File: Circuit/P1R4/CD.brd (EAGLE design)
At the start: 59.7 x 59.7 mm, 126 parts, among them U1 MK20DX256VLH7, U2 TPS61200, U3 MPU-9250, Y1 32.768KHz, Y2 16Mhz/8pF, Y3 26 Mhz, Y4 16 Mhz

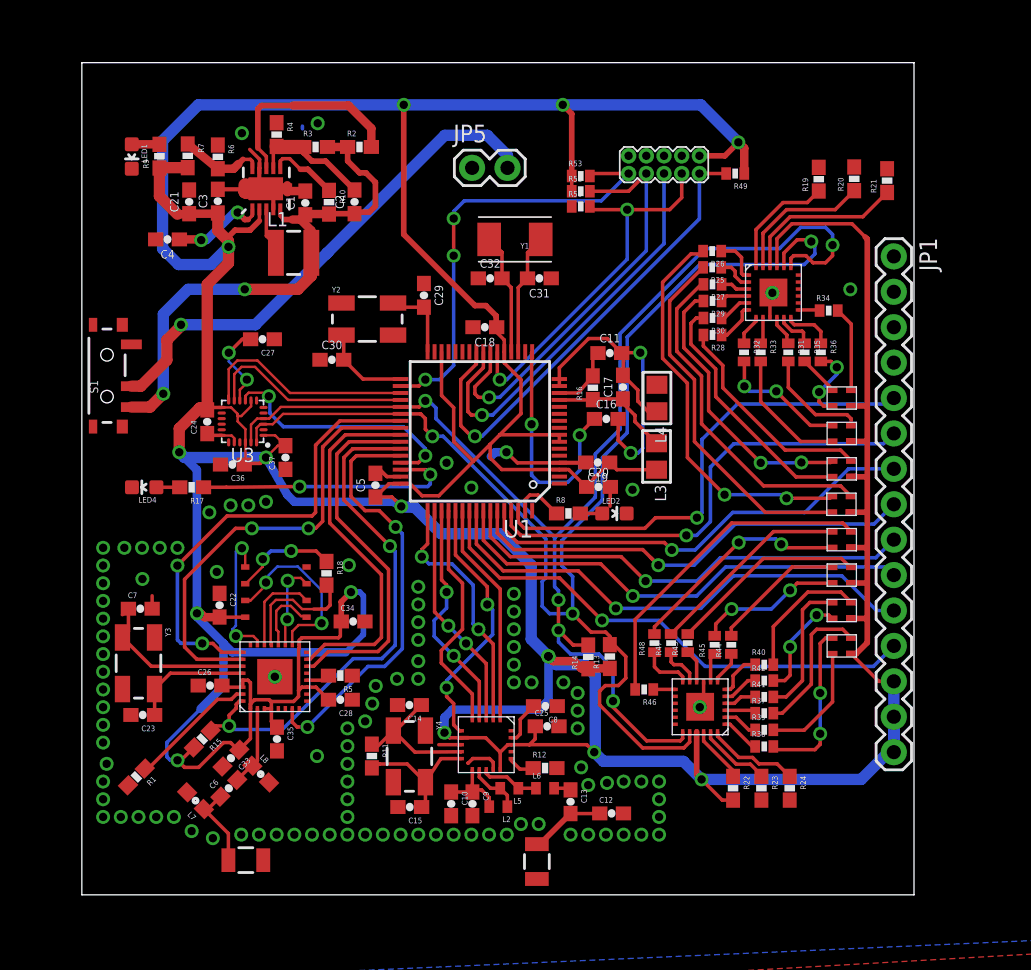
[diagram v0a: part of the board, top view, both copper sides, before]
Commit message: Fixed Wifi wiring, mild rearranging of IO. Pinout documented on Google. Antennae isolated and via fenced
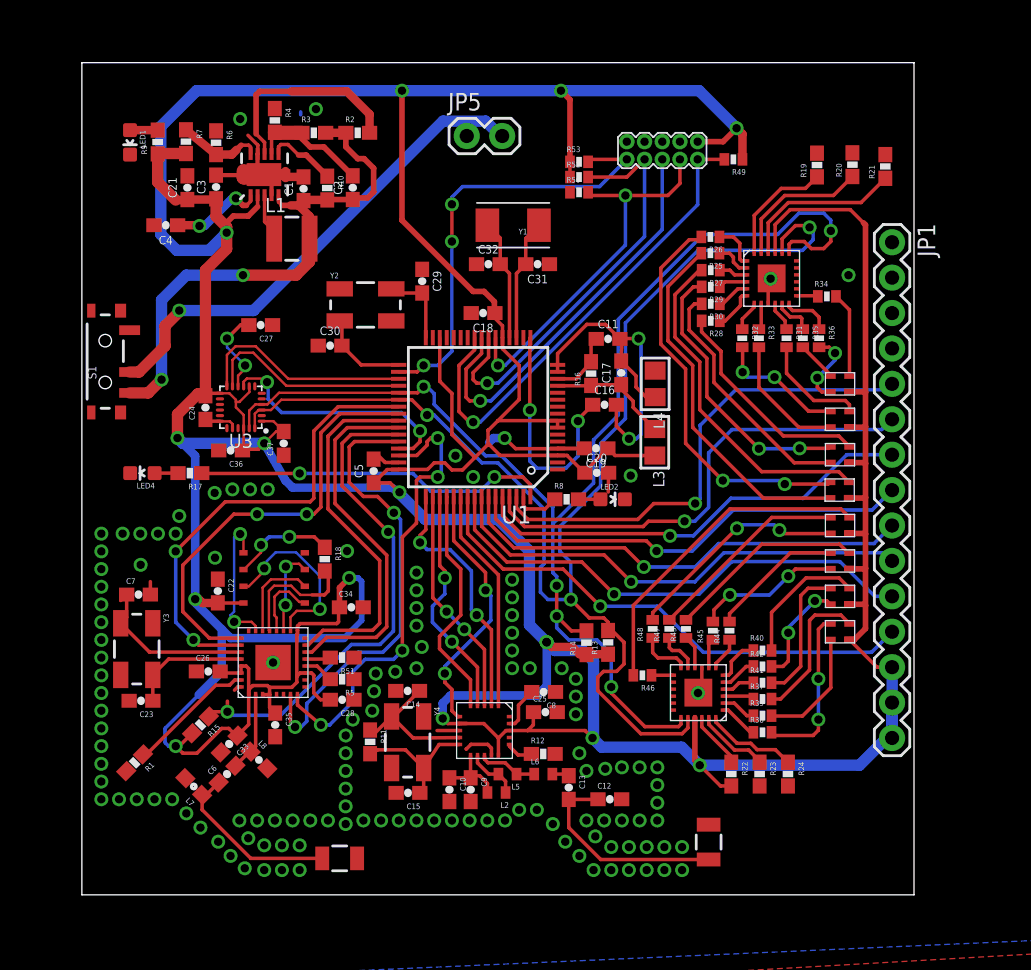
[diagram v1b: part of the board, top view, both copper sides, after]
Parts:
- added R51: 10k, SparkFun-Resistors:0603-RES
- moved U$2 12.4 mm to (45.0, 3.78), turned to 180 degrees
- moved U$1 6.73 mm to (18.5, 2.62)
- moved JP5 2.32 mm to (27.6, 54.4)
- moved C30 1.02 mm to (17.8, 39.4)
- moved R16 1.02 mm to (36.5, 37.4)
- moved R29 1.02 mm to (45.1, 43.6)
- moved R31 1.02 mm to (50.5, 39.9)
- moved R33 1.02 mm to (48.6, 39.9)
- moved R34 1.02 mm to (53.4, 42.9)
- moved R35 1.02 mm to (51.7, 39.9)
- moved R53 1.02 mm to (35.7, 52.6)
- moved U$20 1.02 mm to (49.5, 44.2)
- moved C24 1.02 mm to (8.86, 35.0)
- moved L1 1.02 mm to (15.1, 47.1)
- moved R2 1.02 mm to (19.8, 54.7)
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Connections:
- removed net N$9: R17.1, U1.46
- new net N$8: R51.2, U$6.MTDO/13
- new net PTC3: U$6.XPD_DCDC/8, U1.46
- net GND: now also R51.1
- net PTB16: now also U$6.U0TXD/26; no longer U$6.U0RXD/25
- net PTB17: now also U$6.U0RXD/25; no longer U$6.U0TXD/26
- net PTD7: now also R17.1
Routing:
- net PTC3: track 0.00 -> 33.0 mm, vias 0 -> 4
- net PTD7: track 0.00 -> 25.6 mm, vias 0 -> 2
- net N$9: track 19.3 -> 0.00 mm, vias 2 -> 0
- net N$26: track 5.42 -> 15.1 mm
- net N$16: track 5.65 -> 12.7 mm
- net PTC1: track 30.6 -> 32.8 mm
- net N$8: track 0.00 -> 1.85 mm
- net 3.3V: track 432.0 -> 433.6 mm
- net PTB17: track 32.5 -> 31.4 mm
- net PTC0: track 37.6 -> 36.6 mm
- net PTD2: track 33.6 -> 32.8 mm
- net SCL: track 93.6 -> 94.3 mm
- net N$32: track 1.68 -> 2.19 mm
- net GND: vias 103 -> 126

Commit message: Preliminary Final R4 finished
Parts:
- moved C8 0.13 mm to (33.2, 14.6)
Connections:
- net N$8 renamed MTDO
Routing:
- net 3.3V: track 433.6 -> 419.4 mm, vias 15 -> 14
- net PTC0: track 36.6 -> 37.6 mm
- net PTC8: track 18.8 -> 19.4 mm
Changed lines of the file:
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@@
 <element name="C23" library="SparkFun-Capacitors" package="0603-CAP" value="15 pF" x="4.2418" y="13.9192" rot="R180"/>
 <element name="C7" library="SparkFun-Capacitors" package="0603-CAP" value="15 pF" x="4.064" y="21.5392"/>
-<element name="C8" library="SparkFun-Capacitors" package="0603-CAP" value="33 nF" x="33.1216" y="14.5542" rot="R180"/>
+<element name="C8" library="SparkFun-Capacitors" package="0603-CAP" value="33 nF" x="33.2486" y="14.5542" rot="R180"/>
 <element name="C13" library="SparkFun-Capacitors" package="0603-CAP" value="1.5 pF" x="34.925" y="7.6962" rot="R270"/>
 <element name="C12" library="SparkFun-Capacitors" package="0603-CAP" value="1.0 pF" x="37.8714" y="6.858"/>
@@
 <contactref element="C16" pad="1"/>
 <via x="35.5854" y="33.9852" extent="1-16" drill="0.6"/>
-<via x="32.131" y="34.7726" extent="1-16" drill="0.6"/>
 <wire x1="36.6404" y1="35.1536" x2="35.5854" y2="34.0986" width="0.254" layer="1"/>
 <wire x1="35.5854" y1="34.0986" x2="35.5854" y2="33.9852" width="0.254" layer="1"/>
@@
 <wire x1="35.5854" y1="31.4706" x2="35.5854" y2="33.9852" width="0.254" layer="16"/>
 <wire x1="34.7218" y1="30.607" x2="32.639" y2="30.607" width="0.254" layer="16"/>
-<wire x1="32.639" y1="30.607" x2="32.131" y2="31.115" width="0.254" layer="16"/>
-<wire x1="32.131" y1="31.115" x2="32.131" y2="34.7726" width="0.254" layer="16"/>
-<wire x1="32.1726" y1="39.9646" x2="32.131" y2="39.923" width="0.254" layer="1"/>
-<wire x1="32.131" y1="39.923" x2="32.131" y2="34.7726" width="0.254" layer="1"/>
+<wire x1="32.1726" y1="39.9646" x2="32.1726" y2="32.9784" width="0.254" layer="1"/>
+<wire x1="32.1726" y1="32.9784" x2="32.258" y2="32.893" width="0.254" layer="1"/>
+<via x="32.258" y="32.893" extent="1-16" drill="0.6"/>
+<wire x1="32.258" y1="32.893" x2="32.258" y2="30.988" width="0.254" layer="16"/>
+<wire x1="32.258" y1="30.988" x2="32.639" y2="30.607" width="0.254" layer="16"/>
 </signal>
 <signal name="N$27">
@@
 <contactref element="U$6" pad="EXT_RSTB/32"/>
 <wire x1="11.416" y1="14.9124" x2="11.1786" y2="14.9124" width="0.254" layer="1"/>
-<wire x1="11.1786" y1="14.9124" x2="10.9474" y2="14.6812" width="0.254" layer="1"/>
 <wire x1="22.7226" y1="33.0146" x2="19.2986" y2="33.0146" width="0.254" layer="1"/>
 <wire x1="19.2986" y1="33.0146" x2="18.669" y2="32.385" width="0.254" layer="1"/>
@@
 <wire x1="14.2494" y1="12.8778" x2="10.6934" y2="12.8778" width="0.254" layer="16"/>
 <wire x1="10.6934" y1="12.8778" x2="10.4394" y2="13.1318" width="0.254" layer="16"/>
-<wire x1="10.4394" y1="13.8938" x2="10.4394" y2="13.1318" width="0.254" layer="1"/>
+<wire x1="10.4394" y1="13.8938" x2="10.4394" y2="13.716" width="0.254" layer="1"/>
+<wire x1="10.4394" y1="13.716" x2="10.4394" y2="13.1318" width="0.254" layer="1"/>
 <wire x1="18.669" y1="29.337" x2="18.669" y2="32.385" width="0.254" layer="1"/>
 <wire x1="19.3294" y1="17.9578" x2="14.2494" y2="12.8778" width="0.254" layer="16"/>
@@
 <wire x1="9.110040625" y1="12.793040625" x2="9.4488" y2="13.1318" width="0.254" layer="1"/>
 <wire x1="9.4488" y1="13.1318" x2="10.4394" y2="13.1318" width="0.254" layer="1"/>
-<wire x1="10.4394" y1="13.8938" x2="10.9474" y2="14.6812" width="0" layer="19" extent="1-1"/>
+<wire x1="11.1786" y1="14.9124" x2="10.4394" y2="14.1732" width="0.254" layer="1"/>
+<wire x1="10.4394" y1="14.1732" x2="10.4394" y2="13.8938" width="0.254" layer="1"/>
 </signal>
 <signal name="PTD1">
@@
 <wire x1="31.0562" y1="12.2856" x2="31.3182" y2="12.5476" width="0.254" layer="1"/>
 <wire x1="31.3182" y1="12.5476" x2="31.3182" y2="13.6008" width="0.254" layer="1"/>
-<wire x1="31.3182" y1="13.6008" x2="32.2716" y2="14.5542" width="0.254" layer="1"/>
 <contactref element="U$4" pad="19"/>
 <wire x1="30.6798" y1="12.2856" x2="31.0562" y2="12.2856" width="0.254" layer="1"/>
+<wire x1="31.3182" y1="13.6008" x2="32.2716" y2="14.5542" width="0.254" layer="1"/>
+<wire x1="32.2716" y1="14.5542" x2="32.3986" y2="14.5542" width="0.254" layer="1"/>
 </signal>
 <signal name="N$23">
@@
 <wire x1="26.035" y1="16.383" x2="29.337" y2="19.685" width="0.254" layer="16"/>
 <wire x1="26.035" y1="15.875" x2="26.035" y2="15.24" width="0.254" layer="1"/>
-<wire x1="26.035" y1="15.24" x2="26.543" y2="14.732" width="0.254" layer="1"/>
-<wire x1="26.543" y1="14.732" x2="26.543" y2="13.208" width="0.254" layer="1"/>
-<wire x1="26.543" y1="13.208" x2="26.9654" y2="12.7856" width="0.254" layer="1"/>
 <wire x1="26.9654" y1="12.7856" x2="27.0798" y2="12.7856" width="0.254" layer="1"/>
+<wire x1="26.9654" y1="12.7856" x2="26.035" y2="13.716" width="0.254" layer="1"/>
+<wire x1="26.035" y1="13.716" x2="26.035" y2="15.875" width="0.254" layer="1"/>
 </signal>
 <signal name="3.3V">
@@
 <wire x1="11.6046" y1="33.4758" x2="11.6046" y2="34.4202" width="0.1778" layer="1"/>
 <via x="22.7838" y="28.8798" extent="1-16" drill="0.6"/>
-<wire x1="13.081" y1="32.385" x2="14.605" y2="29.718" width="0.6096" layer="16"/>
 <wire x1="9.7638" y1="20.933" x2="8.658" y2="20.933" width="0.6096" layer="1"/>
 <via x="8.128" y="21.209" extent="1-16" drill="0.6"/>
@@
 <wire x1="36.6268" y1="11.2522" x2="36.0934" y2="11.7856" width="0.254" layer="1"/>
 <wire x1="36.0934" y1="11.7856" x2="31.9786" y2="11.7856" width="0.254" layer="1"/>
-<via x="25.8826" y="12.6492" extent="1-16" drill="0.6"/>
-<wire x1="26.8986" y1="12.2936" x2="27.6098" y2="12.2936" width="0.254" layer="1"/>
-<wire x1="27.0798" y1="12.2856" x2="26.2462" y2="12.2856" width="0.254" layer="1"/>
-<wire x1="26.2462" y1="12.2856" x2="25.8826" y2="12.6492" width="0.254" layer="1"/>
-<wire x1="32.6644" y1="14.3002" x2="26.4414" y2="14.3002" width="0.6096" layer="16"/>
-<wire x1="26.4414" y1="14.3002" x2="25.8826" y2="13.7414" width="0.6096" layer="16"/>
-<wire x1="25.8826" y1="13.7414" x2="25.8826" y2="12.6492" width="0.6096" layer="16"/>
-<wire x1="27.0798" y1="12.2856" x2="27.0718" y2="12.2936" width="0.1778" layer="1"/>
-<wire x1="27.0718" y1="12.2936" x2="26.8986" y2="12.2936" width="0.1778" layer="1"/>
 <wire x1="44.323" y1="9.2964" x2="55.7784" y2="9.2964" width="0.8128" layer="16"/>
 <wire x1="55.7784" y1="9.2964" x2="58.1152" y2="11.6332" width="0.8128" layer="16"/>
@@
 <wire x1="37.2872" y1="10.5918" x2="43.0276" y2="10.5918" width="0.8128" layer="16"/>
 <wire x1="43.0276" y1="10.5918" x2="44.323" y2="9.2964" width="0.8128" layer="16"/>
-<wire x1="32.6644" y1="14.3002" x2="33.3502" y2="14.986" width="0.6096" layer="16"/>
 <wire x1="22.733" y1="28.829" x2="22.7838" y2="28.8798" width="0.8128" layer="16"/>
 <wire x1="22.7838" y1="28.8798" x2="22.1098" y2="29.5538" width="0.254" layer="1"/>
@@
 <wire x1="15.113" y1="29.21" x2="22.1996" y2="29.21" width="0.6096" layer="16"/>
 <wire x1="22.1996" y1="29.21" x2="22.7838" y2="28.8798" width="0.6096" layer="16"/>
-<wire x1="15.113" y1="29.21" x2="14.605" y2="29.718" width="0.6096" layer="16"/>
 <wire x1="33.3248" y1="18.1356" x2="32.1056" y2="19.3548" width="0.8128" layer="16"/>
 <wire x1="32.1056" y1="19.3548" x2="32.1056" y2="24.6634" width="0.8128" layer="16"/>
 <wire x1="33.3248" y1="18.1356" x2="33.3502" y2="18.1102" width="0.6096" layer="16"/>
-<wire x1="33.3502" y1="18.1102" x2="33.3502" y2="14.986" width="0.6096" layer="16"/>
 <via x="33.3502" y="18.1102" extent="1-16" drill="0.6"/>
 <wire x1="33.3502" y1="18.1102" x2="33.6804" y2="17.78" width="0.6096" layer="1"/>
@@
 <wire x1="26.035" y1="30.988" x2="26.543" y2="30.48" width="0.254" layer="1"/>
 <wire x1="26.543" y1="30.48" x2="27.305" y2="30.48" width="0.254" layer="1"/>
+<wire x1="13.081" y1="32.385" x2="13.081" y2="31.242" width="0.6096" layer="16"/>
+<wire x1="13.081" y1="31.242" x2="15.113" y2="29.21" width="0.6096" layer="16"/>
+<wire x1="33.3502" y1="18.1102" x2="33.401" y2="18.034" width="0" layer="19" extent="1-16"/>
 </signal>
 <signal name="N$3">
@@
 <wire x1="15.7226" y1="12.0396" x2="15.2908" y2="12.0396" width="0.254" layer="16"/>
 </signal>
-<signal name="N$8">
+<signal name="MTDO">
 <contactref element="U$6" pad="MTDO/13"/>
 <contactref element="R51" pad="2"/>
